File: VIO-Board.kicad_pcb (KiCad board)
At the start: 4 copper layers, 39.6 x 39.6 mm, 20 parts, among them J1 Conn_01x02_Female, J2 USB_B_Micro, J3 Conn_01x09_Male, J4 Conn_01x09_Male, J5 Conn_01x09_Male, J6 Conn_01x09_Female, J7 Conn_01x09_Female, J8 Conn_01x09_Female, U1 CP2102N-Axx-xQFN28

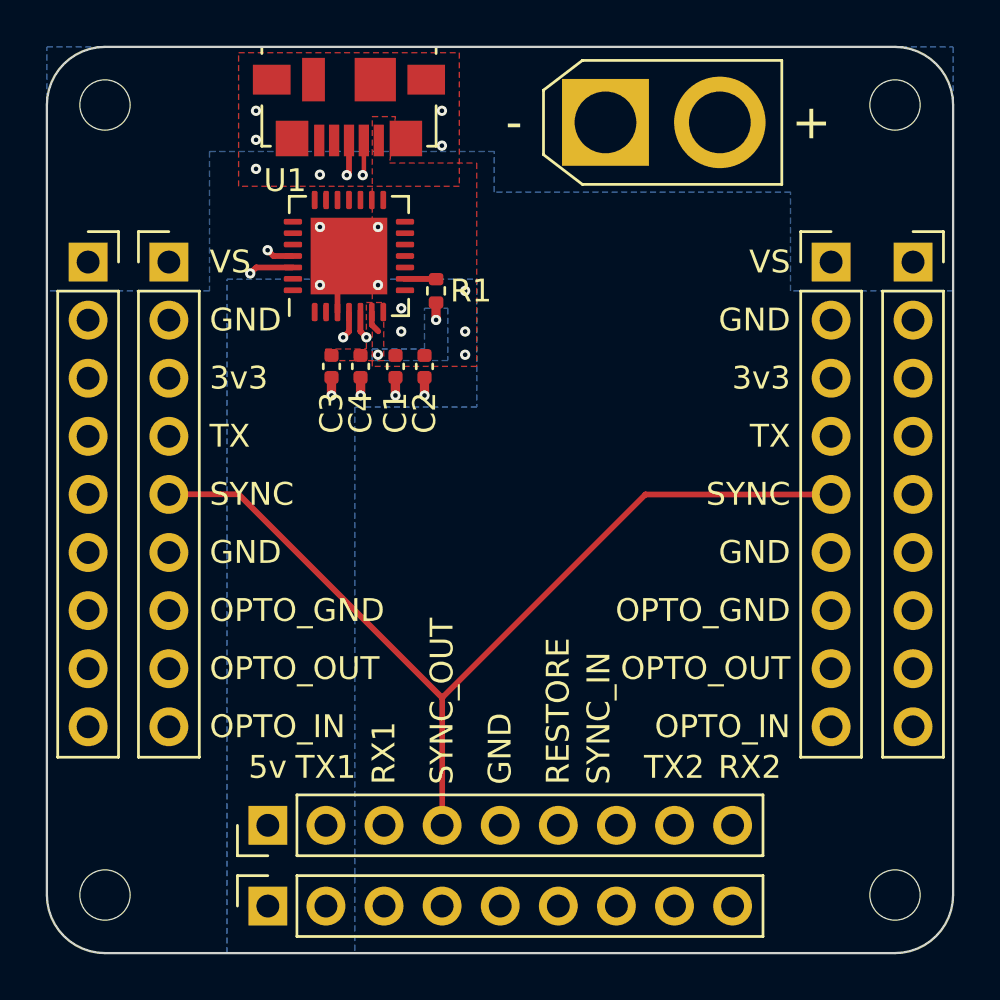
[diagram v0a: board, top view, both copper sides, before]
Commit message: new package, ESD protection, fixes
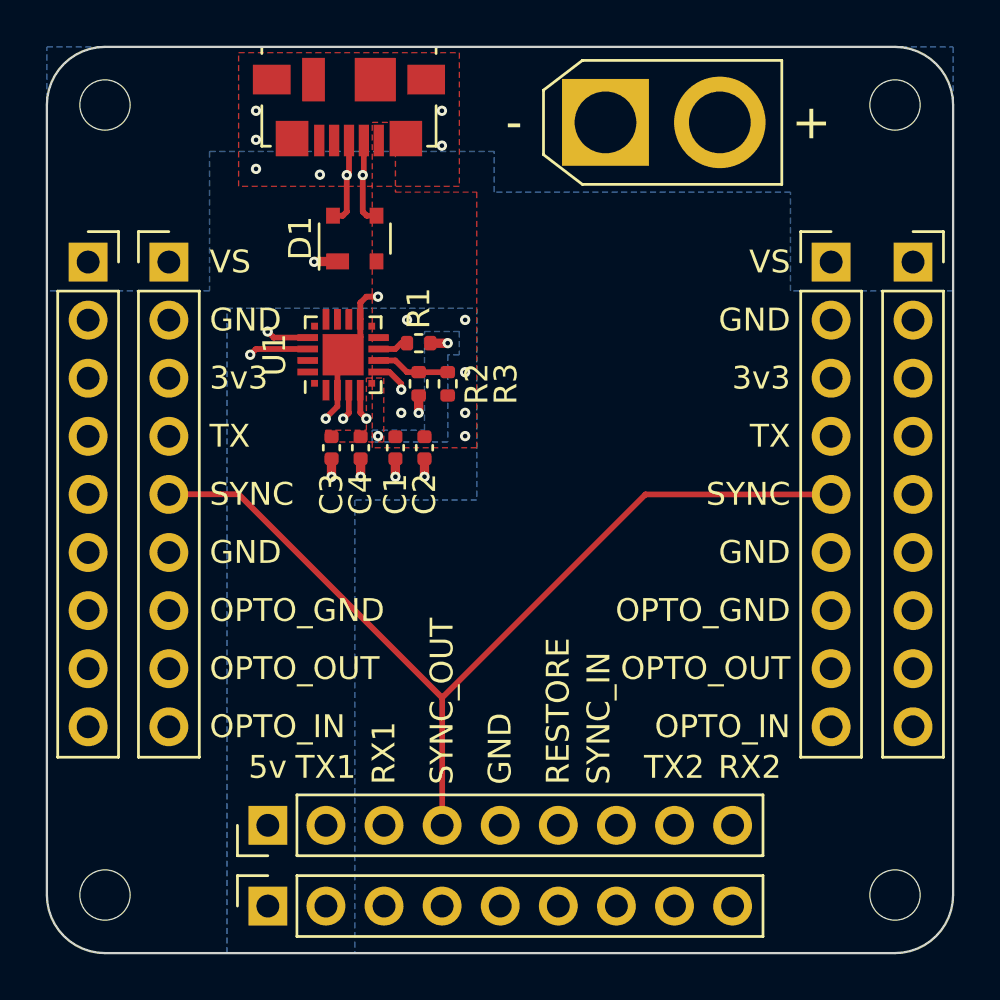
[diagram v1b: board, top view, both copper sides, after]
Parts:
- added D1: SP0503BAHT, Package_TO_SOT_SMD:SOT-143, F.Cu at (70.1, 59.2)
- added R2: 22k1, Resistor_SMD:R_0402_1005Metric, F.Cu at (74.2, 65.5)
- added R3: 47k5, Resistor_SMD:R_0402_1005Metric, F.Cu at (72.9, 65.5)
- U1: value CP2102N-Axx-xQFN28 -> CP2102N-Axx-xQFN20; footprint Package_DFN_QFN:QFN-28-1EP_5x5mm_P0.5mm_EP3.35x3.35mm -> Package_DFN_QFN:SiliconLabs_QFN-20-1EP_3x3mm_P0.5mm_EP1.8x1.8mm
- moved U1 4.33 mm to (69.6, 64.3)
- moved C1 3.56 mm to (71.9, 68.3)
- moved C2 3.56 mm to (73.2, 68.3)
- moved C3 3.56 mm to (69.1, 68.3)
- moved C4 3.56 mm to (70.4, 68.3)
- moved R1 2.41 mm to (72.9, 63.8), turned to 180 degrees
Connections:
- U1 pad 12: unconnected-(U1-Pad12) -> GNDREF
- U1 pad 17: unconnected-(U1-Pad17) -> /RX2
- U1 pad 18: unconnected-(U1-Pad18) -> /TX2
- U1 pad 21: unconnected-(U1-Pad21) -> GNDREF
- U1 pad 8: VBUS -> Net-(R2-Pad2)
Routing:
- net /D+: track 10.1 -> 16.0 mm
- net /D-: track 10.2 -> 16.0 mm
- net GNDREF: track 9.35 -> 15.1 mm
- net Net-(R2-Pad2): track 0.00 -> 3.23 mm
- net /TX2: track 37.3 -> 35.5 mm
- net VBUS: track 0.00 -> 1.46 mm, vias 5 -> 7
- net /RX2: track 38.3 -> 37.3 mm
- net +3V3: track 1.72 -> 0.76 mm

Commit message: BOM and corrections
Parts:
- added G***: LOGO, Adin_Logo:Adin_Logo, B.Cu at (76.5, 72.9)
